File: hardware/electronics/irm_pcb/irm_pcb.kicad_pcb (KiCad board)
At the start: 2 copper layers, 115.1 x 81.3 mm, 63 parts, among them IC1 23LC1024, J1 Conn_01x04, J10 Conn_02x05_Counter_Clockwise, J11 Conn_01x04, J12 Conn_01x06, J13 Conn_01x06, J14 Conn_01x10, J16 Screw_Terminal_01x02, J17 Conn_01x06, J2 JUMPER_OPEN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

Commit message: Rev 1.1
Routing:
- net +3V3: track 671.0 -> 670.5 mm
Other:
- board size 115.1 x 81.3 mm -> 115 x 80.9 mm
- board text added: "CONTRAST"
- board text removed: "CON"

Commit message: Added WROOM decoupling capacitors
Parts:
- added C22: 10u, Capacitor_SMD:C_0805_2012Metric_Pad1.15x1.40mm_HandSolder, F.Cu at (110.0, 51.0)
- added C24: 100n, Capacitor_SMD:C_0805_2012Metric_Pad1.15x1.40mm_HandSolder, F.Cu at (110.0, 48.3)
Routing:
- net +3V3: track 670.5 -> 678.7 mm
- net AGND: track 137.4 -> 141.3 mm, vias 49 -> 51
- net /WROOM Processor/SENSOR_VP: track 42.4 -> 43.0 mm
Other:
- board text added: "+24V"
- board text removed: "24V"

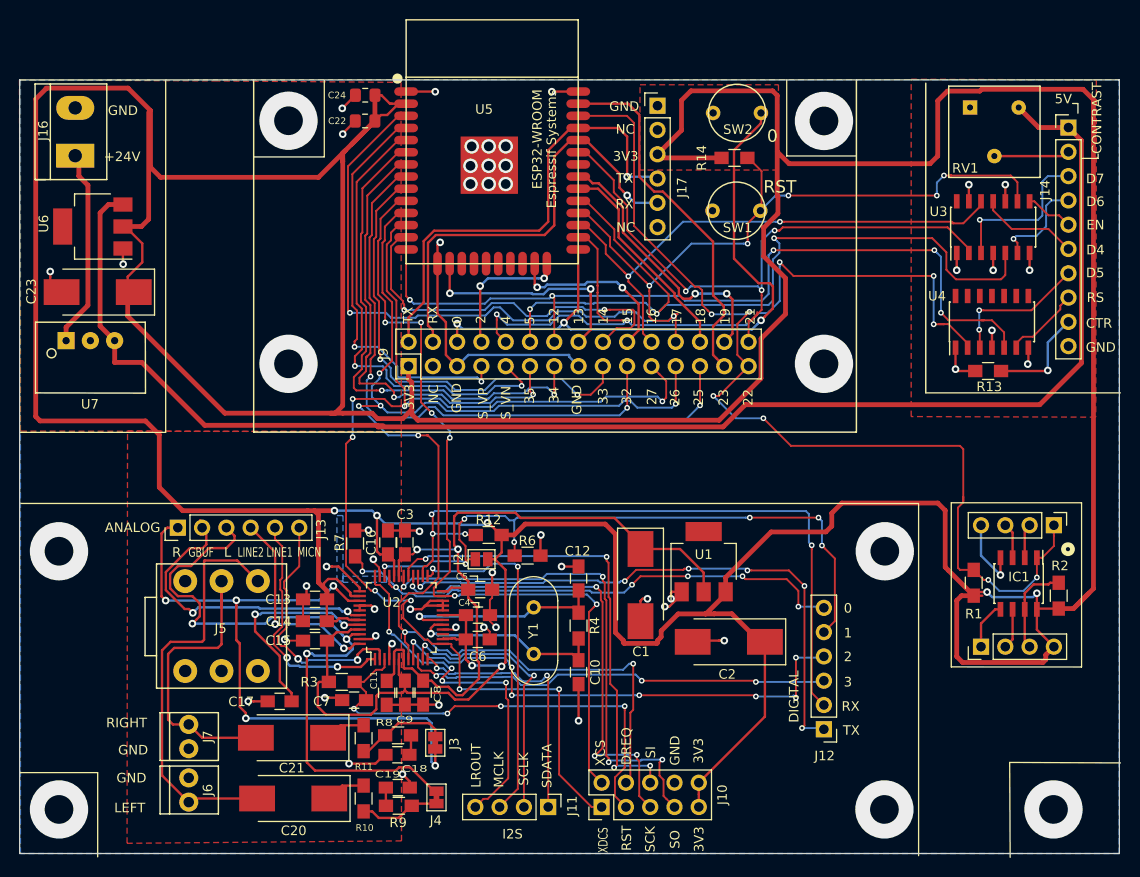
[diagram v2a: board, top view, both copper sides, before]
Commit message: Added 3V3 copper flows
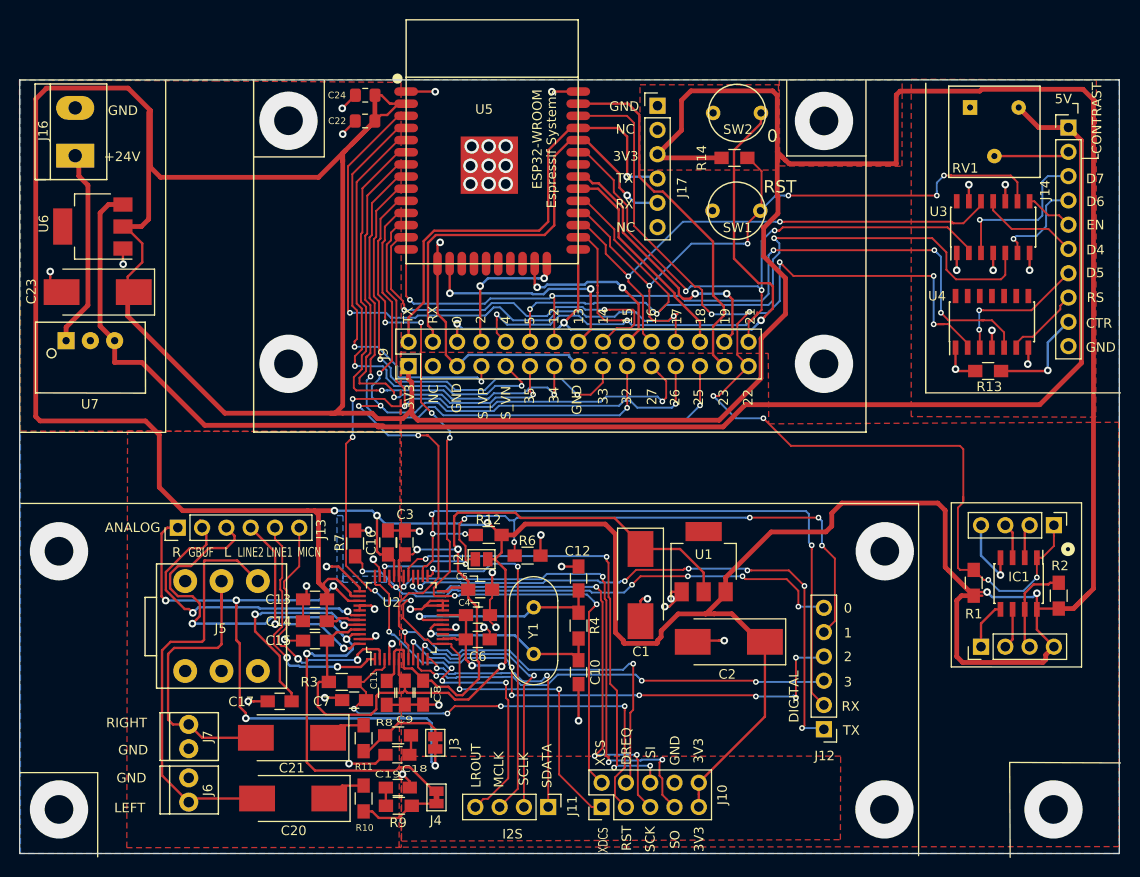
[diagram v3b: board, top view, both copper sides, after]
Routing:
- net +3V3: track 678.7 -> 679.5 mm
